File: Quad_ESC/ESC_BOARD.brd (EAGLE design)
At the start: 139.7 x 40.6 mm, 33 parts, among them U1 SN74CBTLV3257PWR, Y1 ECS-80-S-4X

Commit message: Labeling
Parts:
- removed RSH1: 1 mΩ, INA4181A4:CSS2H-2512
- C10: value 4.7uF -> 100nF
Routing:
- net +12V: track 0.00 -> 66.3 mm
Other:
- board text added: "ROV X12 Quad ESC v1 12/30/2019 Jacob Bobson"
- board text removed: "ROV X12 Quad_ESC Jacob Bobson"
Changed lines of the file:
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@@
 <wire x1="83.82" y1="2.286" x2="88.9" y2="2.286" width="0.254" layer="25"/>
 <wire x1="83.82" y1="38.354" x2="88.9" y2="38.354" width="0.254" layer="25"/>
-<text x="63.754" y="36.83" size="1.27" layer="21">ROV X12 Quad_ESC
+<text x="106.172" y="28.702" size="1.27" layer="21">ROV X12 Quad ESC v1
+12/30/2019
 Jacob Bobson</text>
 </plain>
@@
 <attribute name="PROD_ID" value="CAP-08280" x="68.961" y="14.605" size="1.778" layer="28" rot="MR270" display="off"/>
 </element>
-<element name="C10" library="SparkFun-Capacitors" library_urn="urn:adsk.eagle:library:510" package="0603" package3d_urn="urn:adsk.eagle:package:37414/1" value="4.7uF" x="73.406" y="27.5336" rot="MR90">
+<element name="C10" library="SparkFun-Capacitors" library_urn="urn:adsk.eagle:library:510" package="0603" package3d_urn="urn:adsk.eagle:package:37414/1" value="100nF" x="73.406" y="27.5336" rot="MR90">
 <attribute name="PROD_ID" value="CAP-08280" x="73.406" y="27.5336" size="1.778" layer="28" rot="MR90" display="off"/>
 </element>
@@
 </element>
 <element name="U$1" library="ESC_to_Backplane_Connectors" package="ESC2BACKPLANE_WHOLE" value="ESC2BACKPLANE" x="53.34" y="36.83" rot="R270"/>
-<element name="RSH1" library="INA4181A4" package="CSS2H-2512" value="1 mΩ" x="-2.794" y="-21.336"/>
 </elements>
 <signals>
@@
 <vertex x="94.996" y="8.382"/>
 </polygon>
-<wire x1="54.61" y1="26.67" x2="85.09" y2="15.24" width="0" layer="19" extent="1-1"/>
+<wire x1="46.94" y1="17.16" x2="43.83" y2="17.16" width="0.8128" layer="16"/>
+<wire x1="43.83" y1="17.16" x2="41.91" y2="15.24" width="0.8128" layer="16"/>
+<wire x1="41.91" y1="15.24" x2="41.91" y2="2.032" width="0.8128" layer="16"/>
+<wire x1="41.91" y1="2.032" x2="42.926" y2="1.016" width="0.8128" layer="16"/>
+<wire x1="42.926" y1="1.016" x2="84.328" y2="1.016" width="0.8128" layer="16"/>
+<wire x1="84.328" y1="1.016" x2="85.09" y2="1.778" width="0.8128" layer="16"/>
+<wire x1="85.09" y1="1.778" x2="85.09" y2="5.08" width="0.8128" layer="16"/>
 </signal>
 <signal name="+3V3">
@@
 </signal>
 </signals>
-<errors>
-</errors>
 </board>
 </drawing>

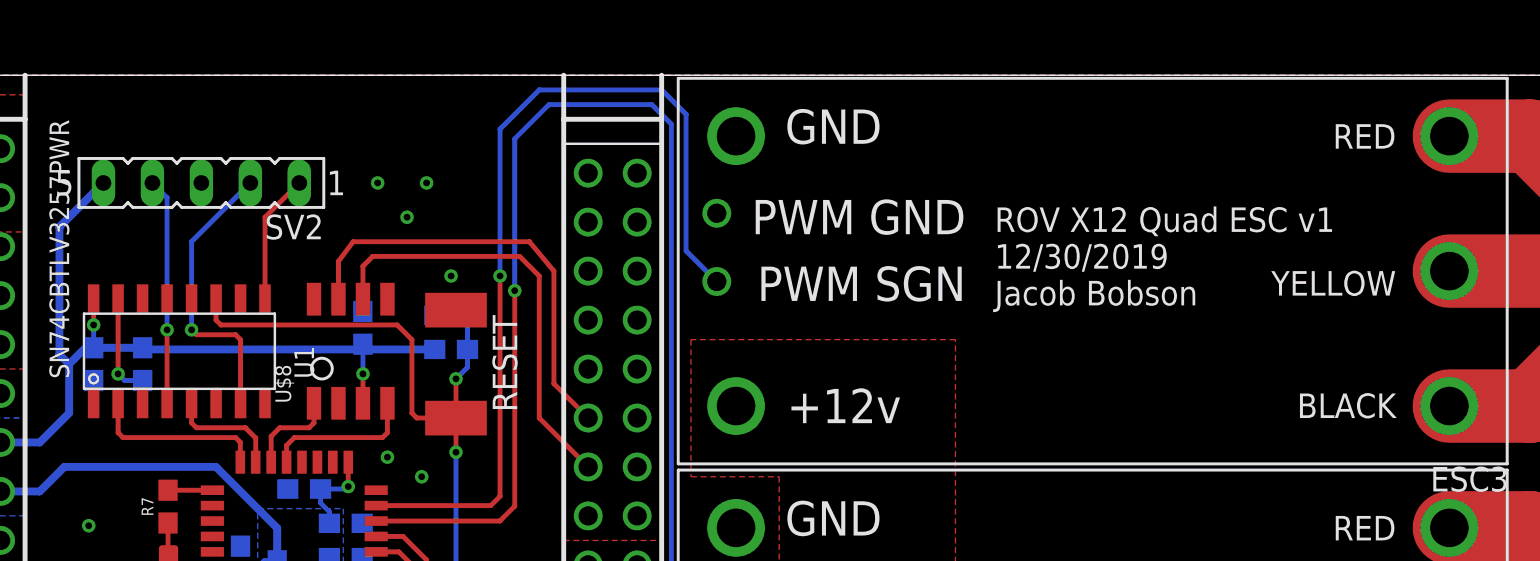
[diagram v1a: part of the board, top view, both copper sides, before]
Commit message: Moved Label
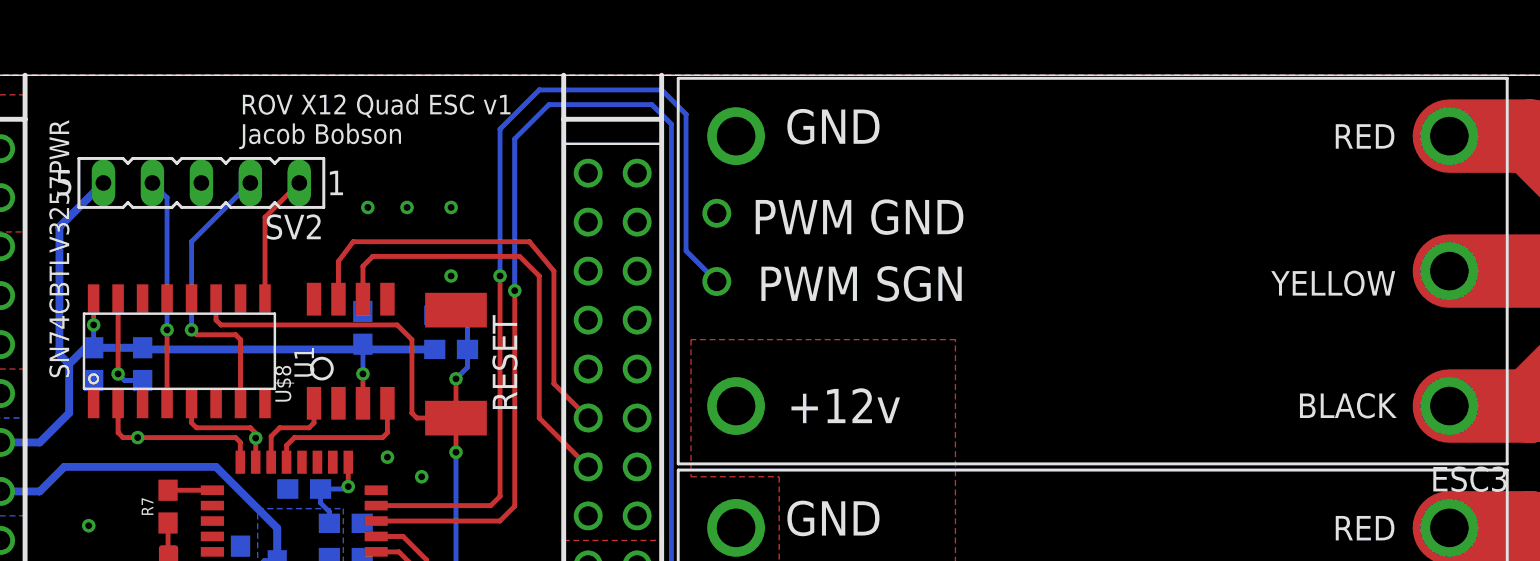
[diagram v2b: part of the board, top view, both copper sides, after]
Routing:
- net SWDIO: track 5.92 -> 6.07 mm, vias 0 -> 1
- net SWCLK: vias 0 -> 1
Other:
- board text added: "ROV X12 Quad ESC v1 Jacob Bobson"
- board text removed: "ROV X12 Quad ESC v1 12/30/2019 Jacob Bobson"
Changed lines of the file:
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@@
 <wire x1="83.82" y1="2.286" x2="88.9" y2="2.286" width="0.254" layer="25"/>
 <wire x1="83.82" y1="38.354" x2="88.9" y2="38.354" width="0.254" layer="25"/>
-<text x="106.172" y="28.702" size="1.27" layer="21">ROV X12 Quad ESC v1
-12/30/2019
+<text x="67.056" y="37.084" size="1.016" layer="21">ROV X12 Quad ESC v1
 Jacob Bobson</text>
 </plain>
@@
 <contactref element="U1" pad="P$5"/>
 <wire x1="67.844" y1="20.565" x2="67.844" y2="21.818" width="0.254" layer="1"/>
-<wire x1="67.844" y1="21.818" x2="67.31" y2="22.352" width="0.254" layer="1"/>
-<wire x1="67.31" y1="22.352" x2="64.77" y2="22.352" width="0.254" layer="1"/>
-<wire x1="64.77" y1="22.352" x2="64.516" y2="22.606" width="0.254" layer="1"/>
+<wire x1="64.516" y1="22.606" x2="64.77" y2="22.352" width="0.254" layer="1"/>
 <wire x1="64.516" y1="22.606" x2="64.516" y2="23.622" width="0.254" layer="1"/>
+<via x="67.844" y="21.818" extent="1-16" drill="0.35"/>
+<wire x1="64.77" y1="22.352" x2="67.564" y2="22.352" width="0.254" layer="1"/>
+<wire x1="67.564" y1="22.352" x2="67.844" y2="22.072" width="0.254" layer="1"/>
+<wire x1="67.844" y1="22.072" x2="67.844" y2="21.818" width="0.254" layer="1"/>
 </signal>
 <signal name="SWCLK">
@@
 <contactref element="U1" pad="P$2"/>
 <wire x1="67.044" y1="20.565" x2="67.044" y2="21.602" width="0.254" layer="1"/>
-<wire x1="67.044" y1="21.602" x2="66.802" y2="21.844" width="0.254" layer="1"/>
-<wire x1="66.802" y1="21.844" x2="60.96" y2="21.844" width="0.254" layer="1"/>
-<wire x1="60.96" y1="21.844" x2="60.706" y2="22.098" width="0.254" layer="1"/>
+<wire x1="66.802" y1="21.844" x2="67.044" y2="21.602" width="0.254" layer="1"/>
+<wire x1="60.706" y1="22.098" x2="60.96" y2="21.844" width="0.254" layer="1"/>
 <wire x1="60.706" y1="22.098" x2="60.706" y2="23.622" width="0.254" layer="1"/>
+<wire x1="60.96" y1="21.844" x2="61.722" y2="21.844" width="0.254" layer="1"/>
+<via x="61.722" y="21.844" extent="1-16" drill="0.35"/>
+<wire x1="61.722" y1="21.844" x2="66.802" y2="21.844" width="0.254" layer="1"/>
 </signal>
 <signal name="OSC_IN">
@@
 </signal>
 <signal name="GND1">
-<via x="74.168" y="35.052" extent="1-16" drill="0.35"/>
+<via x="73.66" y="33.782" extent="1-16" drill="0.35"/>
 </signal>
 <signal name="GND2">
-<via x="76.708" y="35.052" extent="1-16" drill="0.35"/>
+<via x="77.978" y="33.782" extent="1-16" drill="0.35"/>
 </signal>
 <signal name="GND3">
-<via x="75.692" y="33.274" extent="1-16" drill="0.35"/>
+<via x="75.692" y="33.782" extent="1-16" drill="0.35"/>
 </signal>
 <signal name="GND4">

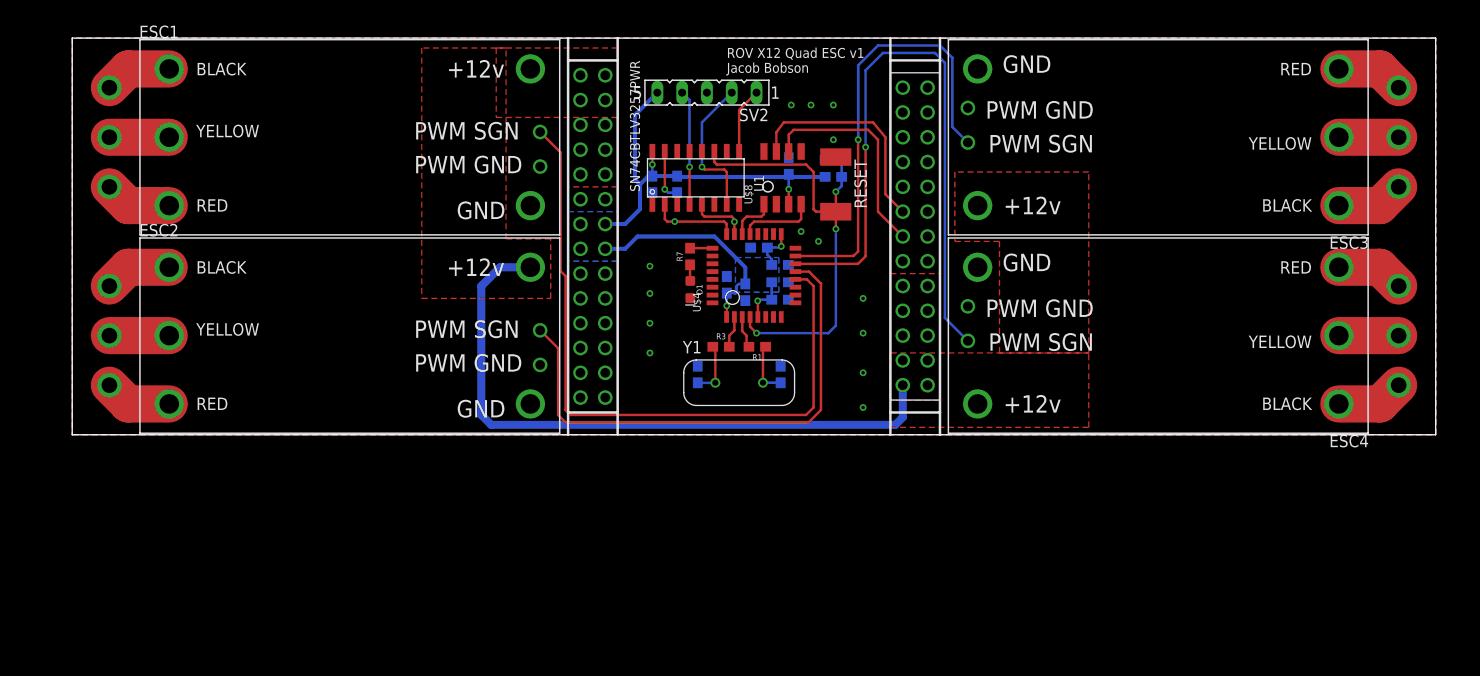
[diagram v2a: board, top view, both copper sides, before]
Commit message: fixed mux and manufacturing errors
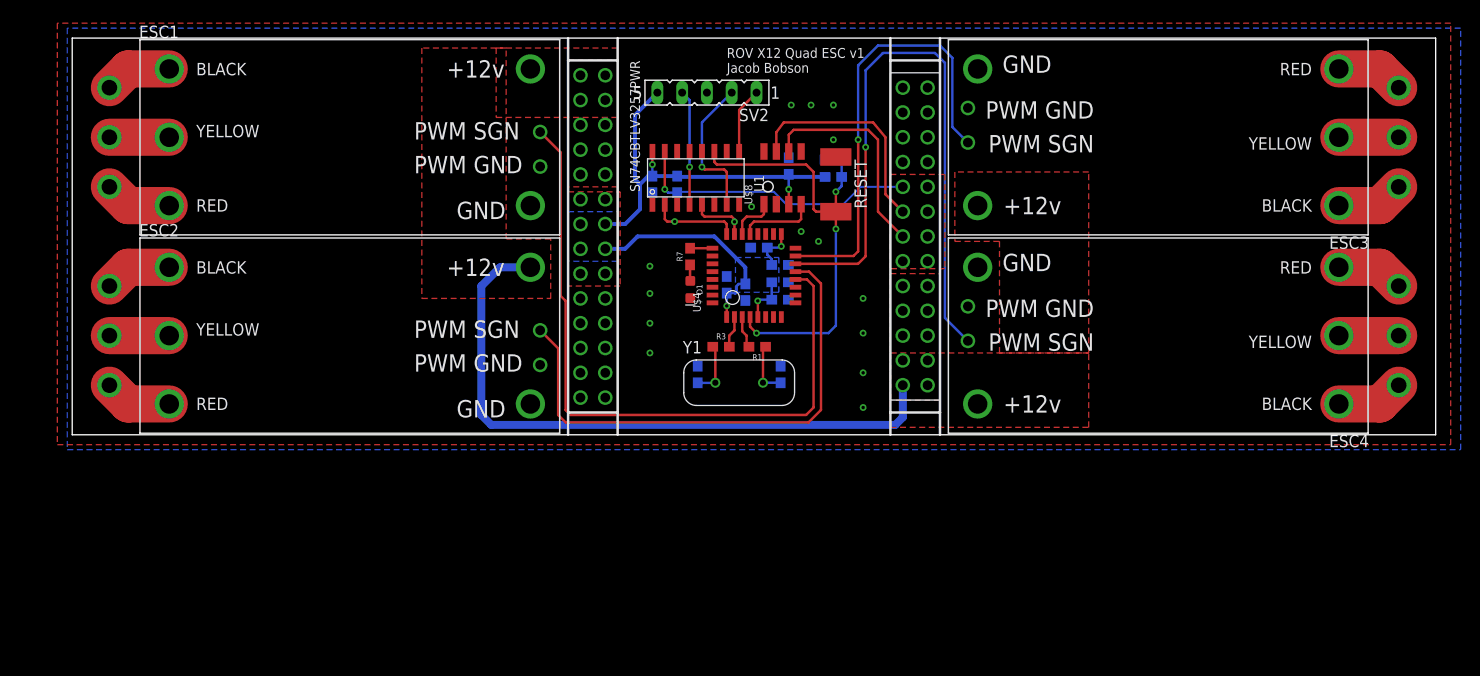
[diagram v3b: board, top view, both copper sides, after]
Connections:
- removed net N$4: R4.1, U1.P$15
- removed net S: U1.P$1
- net GND: now also U1.P$1
- net PROG_SEL: now also R4.1, U1.P$15
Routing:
- net PROG_SEL: track 0.00 -> 29.7 mm, vias 0 -> 1
- net N$4: track 5.29 -> 0.00 mm, vias 1 -> 0
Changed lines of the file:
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@@
 <?xml version="1.0" encoding="utf-8"?>
 <!DOCTYPE eagle SYSTEM "eagle.dtd">
-<eagle version="8.6.1">
+<eagle version="9.1.3">
 <drawing>
 <settings>
@@
 <setting verticaltext="up"/>
 </settings>
-<grid distance="10" unitdist="mil" unit="mil" style="lines" multiple="1" display="yes" altdistance="5" altunitdist="mil" altunit="mil"/>
+<grid distance="10" unitdist="mil" unit="mil" style="lines" multiple="1" display="no" altdistance="5" altunitdist="mil" altunit="mil"/>
 <layers>
 <layer number="1" name="Top" color="4" fill="1" visible="yes" active="yes"/>
@@
 <param name="checkStop" value="0"/>
 <param name="checkValues" value="0"/>
+<param name="checkNames" value="1"/>
+<param name="checkWireStubs" value="1"/>
+<param name="checkPolygonWidth" value="0"/>
 <param name="useDiameter" value="13"/>
 <param name="maxErrors" value="50"/>
@@
 <contactref element="C8" pad="2"/>
 <contactref element="C9" pad="2"/>
-<polygon width="0.2032" layer="1" rank="3">
-<vertex x="0" y="40.64"/>
-<vertex x="0" y="0"/>
-<vertex x="139.7" y="0"/>
-<vertex x="139.7" y="40.64"/>
+<polygon width="0.2032" layer="1" isolate="0.4064" rank="3">
+<vertex x="-1.524" y="42.164"/>
+<vertex x="-1.524" y="-1.016"/>
+<vertex x="141.224" y="-1.016"/>
+<vertex x="141.224" y="42.164"/>
 </polygon>
 <contactref element="U$4" pad="VSS"/>
 <contactref element="SV2" pad="3"/>
-<polygon width="0.2032" layer="16" rank="3">
-<vertex x="0" y="40.64"/>
-<vertex x="0" y="0"/>
-<vertex x="139.7" y="0"/>
-<vertex x="139.7" y="40.64"/>
+<polygon width="0.2032" layer="16" isolate="0.4064" rank="3">
+<vertex x="-0.508" y="41.656"/>
+<vertex x="-0.508" y="-1.524"/>
+<vertex x="142.24" y="-1.524"/>
+<vertex x="142.24" y="41.656"/>
 </polygon>
 <contactref element="U1" pad="P$8"/>
@@
 <via x="74.676" y="20.828" extent="1-16" drill="0.35"/>
 <via x="76.454" y="19.812" extent="1-16" drill="0.35"/>
+<contactref element="U1" pad="P$1"/>
+<via x="69.596" y="23.368" extent="1-16" drill="0.35"/>
+<polygon width="0.1524" layer="1" pour="cutout">
+<vertex x="50.8" y="24.892"/>
+<vertex x="56.134" y="24.892"/>
+<vertex x="56.134" y="15.24"/>
+<vertex x="50.8" y="15.24"/>
+</polygon>
+<polygon width="0.1524" layer="1" pour="cutout">
+<vertex x="83.82" y="26.67"/>
+<vertex x="89.408" y="26.67"/>
+<vertex x="89.408" y="17.018"/>
+<vertex x="83.82" y="17.018"/>
+</polygon>
 </signal>
 <signal name="TIM3_CH1">
@@
 <wire x1="75.184" y1="2.032" x2="51.054" y2="2.032" width="0.254" layer="1"/>
 <wire x1="51.054" y1="2.032" x2="50.546" y2="2.54" width="0.254" layer="1"/>
-<wire x1="50.546" y1="2.54" x2="50.546" y2="16.256" width="0.254" layer="1"/>
-<wire x1="50.546" y1="16.256" x2="50.038" y2="16.764" width="0.254" layer="1"/>
-<wire x1="50.038" y1="16.764" x2="50.038" y2="28.922" width="0.254" layer="1"/>
+<wire x1="50.546" y1="2.54" x2="50.546" y2="13.716" width="0.254" layer="1"/>
+<wire x1="50.546" y1="13.716" x2="50.038" y2="14.224" width="0.254" layer="1"/>
+<wire x1="50.038" y1="14.224" x2="50.038" y2="28.922" width="0.254" layer="1"/>
 <wire x1="50.038" y1="28.922" x2="47.94" y2="31.02" width="0.254" layer="1"/>
 </signal>
@@
 <contactref element="U$1" pad="P$R"/>
 <contactref element="U$1" pad="P$S"/>
-<polygon width="0.2032" layer="1">
+<polygon width="0.3048" layer="1" isolate="0.4064" rank="2">
 <vertex x="55.88" y="25.4"/>
 <vertex x="50.8" y="25.4"/>
@@
 <vertex x="55.88" y="38.354"/>
 </polygon>
-<polygon width="0.2032" layer="1">
+<polygon width="0.3048" layer="1" isolate="0.4064" rank="2">
 <vertex x="83.82" y="3.556"/>
 <vertex x="83.82" y="16.51"/>
@@
 <vertex x="88.9" y="3.556"/>
 </polygon>
-<polygon width="0.2032" layer="1">
+<polygon width="0.3048" layer="1" isolate="0.4064" rank="2">
 <vertex x="43.434" y="39.624"/>
 <vertex x="43.434" y="32.512"/>
@@
 <contactref element="U$1" pad="P$24"/>
 <contactref element="U$1" pad="P$23"/>
-<polygon width="0.2032" layer="1">
+<polygon width="0.3048" layer="1" isolate="0.4064" rank="2">
 <vertex x="44.45" y="39.624"/>
 <vertex x="35.814" y="39.624"/>
@@
 <vertex x="44.45" y="20.066"/>
 </polygon>
-<polygon width="0.2032" layer="1">
+<polygon width="0.3048" layer="1" isolate="0.4064" rank="2">
 <vertex x="83.82" y="8.382"/>
 <vertex x="83.82" y="0.762"/>
@@
 <vertex x="104.14" y="8.382"/>
 </polygon>
-<polygon width="0.2032" layer="1">
+<polygon width="0.3048" layer="1" isolate="0.4064" rank="2">
 <vertex x="104.14" y="8.382"/>
 <vertex x="104.14" y="26.924"/>
@@
 <wire x1="90.17" y1="31.53" x2="91.76" y2="29.94" width="0.254" layer="16"/>
 </signal>
-<signal name="S">
-<contactref element="U1" pad="P$1"/>
-</signal>
-<signal name="N$4">
-<contactref element="U1" pad="P$15"/>
-<contactref element="R4" pad="1"/>
-<wire x1="61.976" y1="24.804" x2="61.048" y2="24.804" width="0.254" layer="16"/>
-<wire x1="61.048" y1="24.804" x2="60.706" y2="25.146" width="0.254" layer="16"/>
-<via x="60.706" y="25.146" extent="1-16" drill="0.35"/>
-<wire x1="60.706" y1="25.146" x2="60.706" y2="29.022" width="0.254" layer="1"/>
-</signal>
 <signal name="SWCLK_IN">
 <contactref element="U1" pad="P$4"/>
@@
 <signal name="PROG_SEL">
 <contactref element="U$1" pad="P$5"/>
+<contactref element="U1" pad="P$15"/>
+<contactref element="R4" pad="1"/>
+<wire x1="61.976" y1="24.804" x2="61.048" y2="24.804" width="0.254" layer="16"/>
+<wire x1="61.048" y1="24.804" x2="60.706" y2="25.146" width="0.254" layer="16"/>
+<via x="60.706" y="25.146" extent="1-16" drill="0.35"/>
+<wire x1="60.706" y1="25.146" x2="60.706" y2="29.022" width="0.254" layer="1"/>
+<wire x1="85.09" y1="25.4" x2="80.772" y2="25.4" width="0.2032" layer="16"/>
+<wire x1="80.772" y1="25.4" x2="78.994" y2="23.622" width="0.2032" layer="16"/>
+<wire x1="78.994" y1="23.622" x2="73.152" y2="23.622" width="0.2032" layer="16"/>
+<wire x1="73.152" y1="23.622" x2="71.882" y2="24.892" width="0.2032" layer="16"/>
+<wire x1="62.064" y1="24.892" x2="61.976" y2="24.804" width="0.2032" layer="16"/>
+<wire x1="71.882" y1="24.892" x2="62.064" y2="24.892" width="0.2032" layer="16"/>
 </signal>
 <signal name="GND1">
@@
 </signal>
 </signals>
+<mfgpreviewcolors>
+<mfgpreviewcolor name="soldermaskcolor" color="0xC8008000"/>
+<mfgpreviewcolor name="silkscreencolor" color="0xFFFEFEFE"/>
+<mfgpreviewcolor name="backgroundcolor" color="0xFF282828"/>
+<mfgpreviewcolor name="coppercolor" color="0xFFFFBF00"/>
+<mfgpreviewcolor name="substratecolor" color="0xFF786E46"/>
+</mfgpreviewcolors>
 </board>
 </drawing>

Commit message: CAD for ESC board
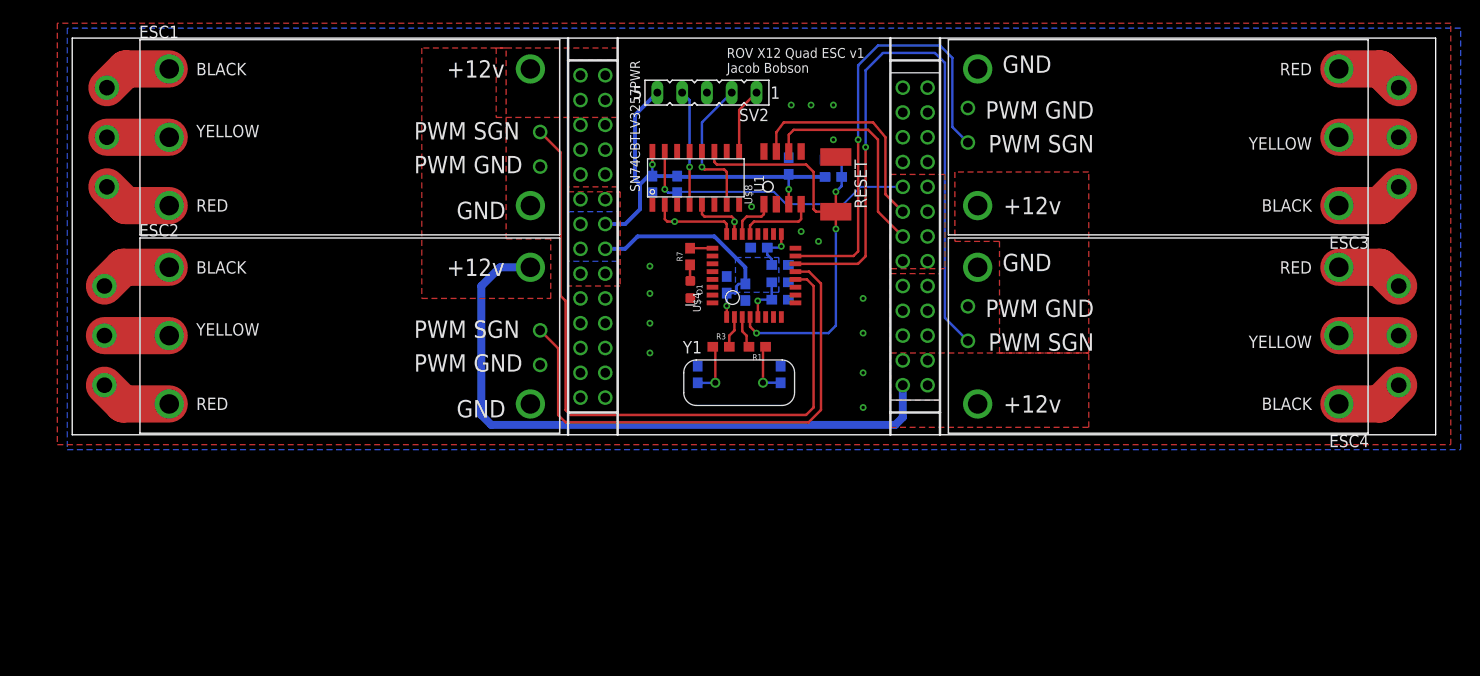
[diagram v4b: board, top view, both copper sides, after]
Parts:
- moved ESC2_CON 0.51 mm to (3.30, 10.2), turned to 270 degrees
- moved ESC1_CON 0.25 mm to (3.56, 30.5), turned to 270 degrees
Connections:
- net ESC1_B: now also ESC1_CON.A; no longer ESC1_CON.C
- net ESC1_R: now also ESC1_CON.C; no longer ESC1_CON.A
- net ESC2_B: now also ESC2_CON.A; no longer ESC2_CON.C
- net ESC2_R: now also ESC2_CON.C; no longer ESC2_CON.A
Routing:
- net ESC2_Y: track 6.13 -> 6.64 mm
- net ESC2_R: track 6.93 -> 7.43 mm
- net ESC2_B: track 6.93 -> 7.43 mm
